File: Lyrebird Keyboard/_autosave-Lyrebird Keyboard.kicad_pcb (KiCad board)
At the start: 4 copper layers, 95 parts, among them IC1 L7915CV, IC2 L78S15CV, IC3 MCP6022-E_SN, IC4 IR2113SPBF, IC5 IR2113SPBF, IC6 LM358DT, IC7 L7805ACD2T-TR, J1 WAV/ENV 4, J10 AC IN 2, J11 240V Out, J12 240 In, J13 MC-254-16-00-ST-DIP, J14 MC-254-16-00-ST-DIP, J15 MC-254-16-00-ST-DIP, J16 MC-254-16-00-ST-DIP, J17 MC-254-16-00-ST-DIP, J18 MC-254-16-00-ST-DIP, J19 MC-254-16-00-ST-DIP, J2 WAV/ENV 3, J20 AMP Out, J21 SUB Out, J3 WAV/ENV 2, J4 WAV/ENV 1, J5 TONE SRC 4, J6 TONE SRC 3, J7 TONE SRC 2, J8 TONE SRC 1, J9 AC IN 1, Q1 BC848, Q2 BC848, Q3 IRFR2905ZTRPBF, Q4 IRFR2905ZTRPBF, Q5 IRFR2905ZTRPBF, Q6 IRFR2905ZTRPBF, U1 DF06S

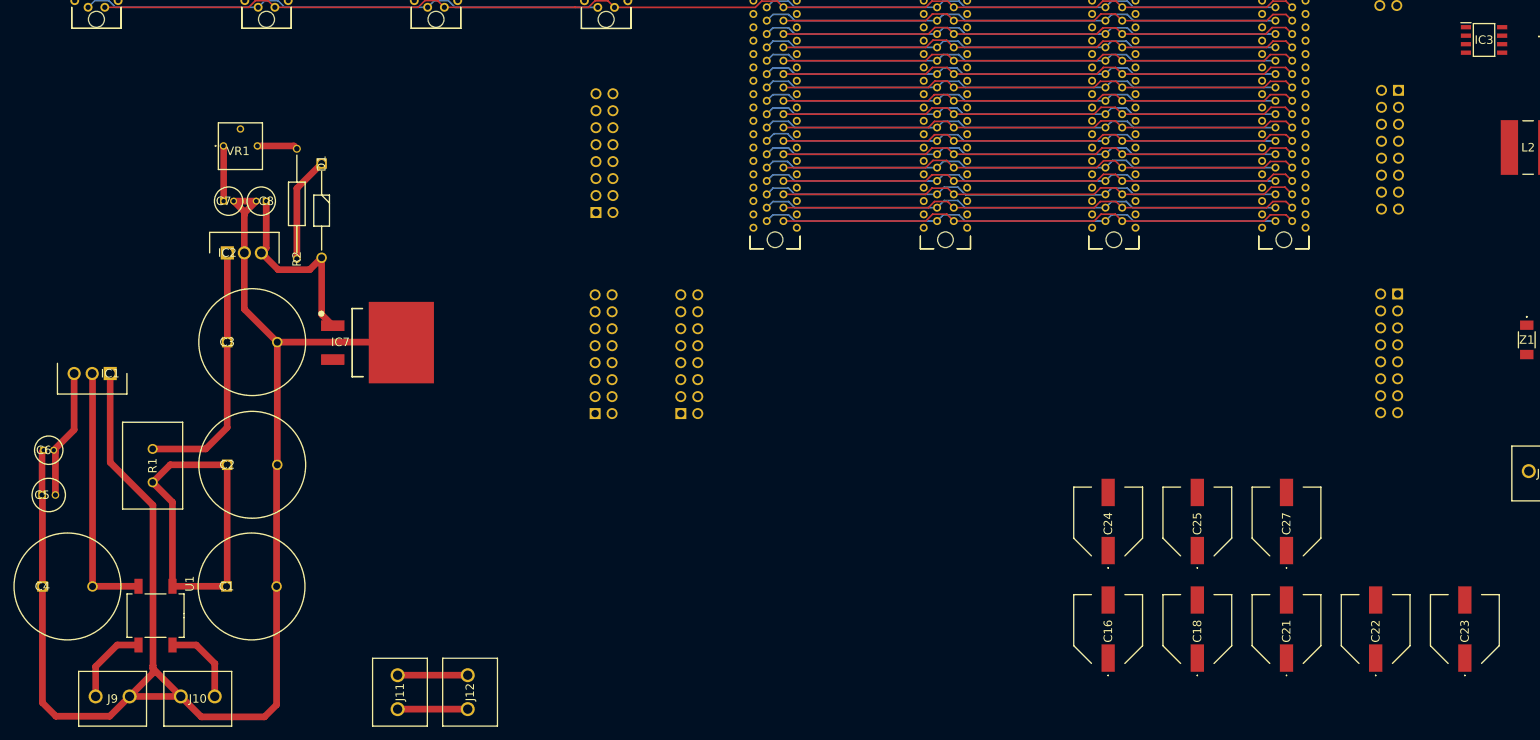
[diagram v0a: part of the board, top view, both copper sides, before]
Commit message: Added schematic definitions
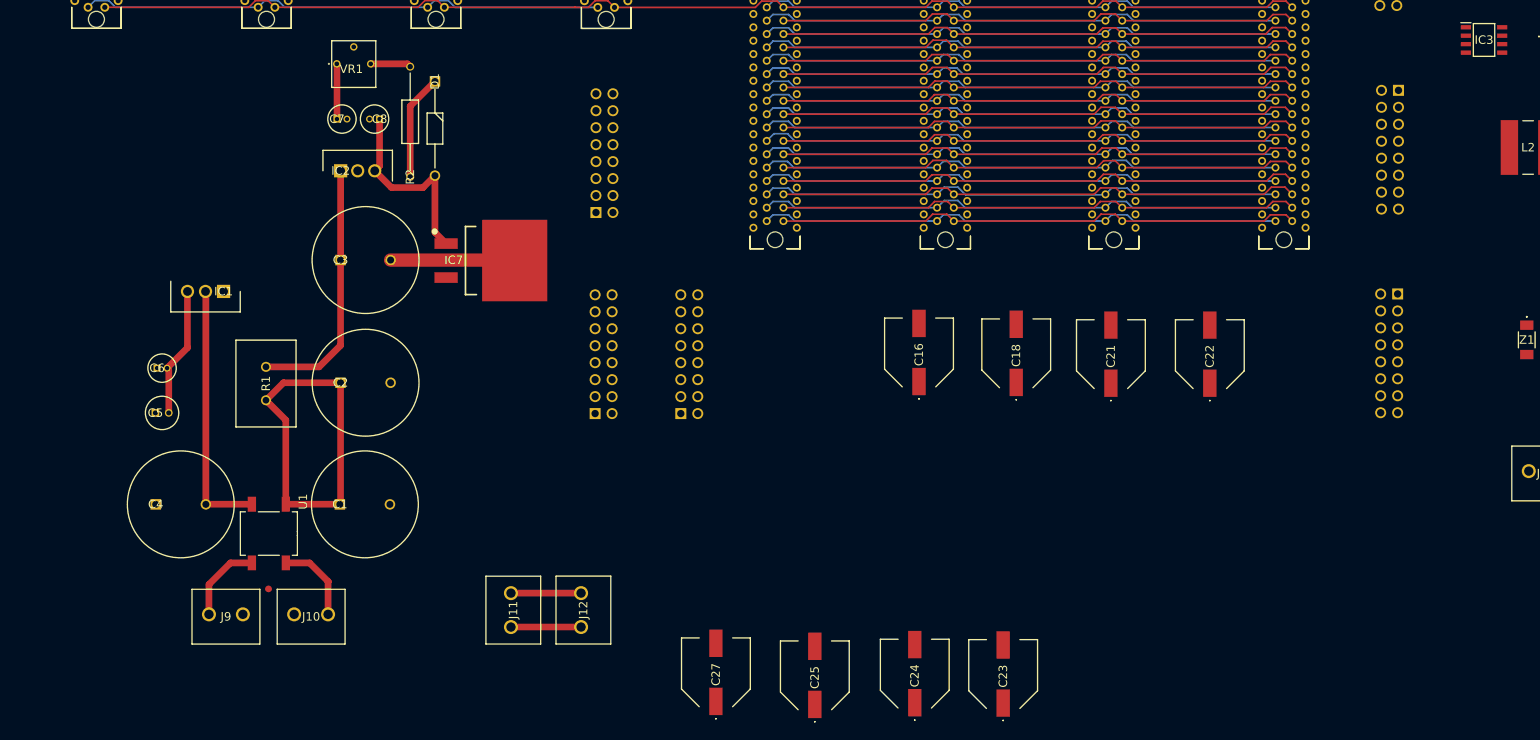
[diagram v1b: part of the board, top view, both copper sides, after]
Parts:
- moved C27 88.4 mm to (123.0, 178.8)
- moved C23 69.4 mm to (166.0, 179.1)
- moved C25 61.7 mm to (137.8, 179.3)
- moved C16 50.2 mm to (153.4, 130.9)
- moved C18 49.4 mm to (167.9, 131.1)
- moved C21 48.8 mm to (182.1, 131.2)
- moved C22 48.1 mm to (196.9, 131.2)
- moved C24 36.8 mm to (152.8, 179.0)
- moved C1 20.9 mm to (66.7, 153.7)
- moved IC1 20.9 mm to (49.3, 121.8)
- moved J11 20.9 mm to (92.3, 172.0)
- moved J12 20.9 mm to (102.8, 172.0)
- moved C4 20.9 mm to (39.1, 153.7)
- moved C5 20.9 mm to (39.1, 140.0)
- moved C6 20.9 mm to (39.3, 133.3)
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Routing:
- net GND: track 238.7 -> 18.9 mm
